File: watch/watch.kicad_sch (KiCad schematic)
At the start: 1 part, among them U1 nRF52840

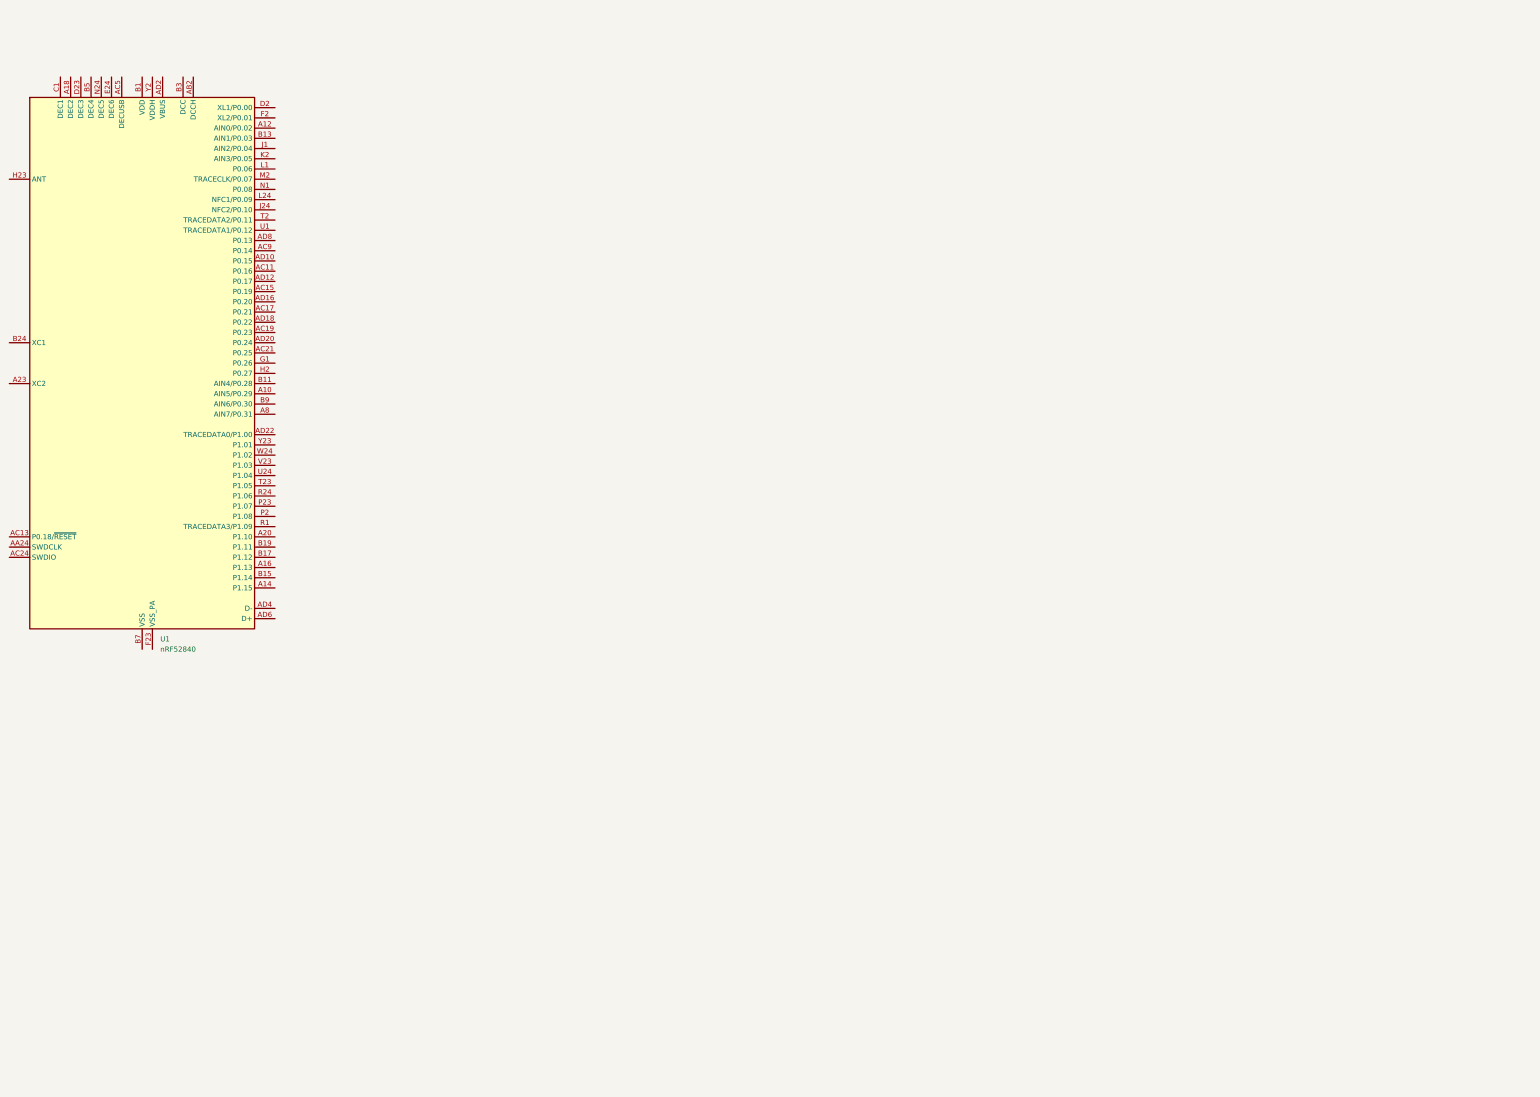
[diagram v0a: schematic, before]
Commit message: lots of stuff: power management, uC power, USB
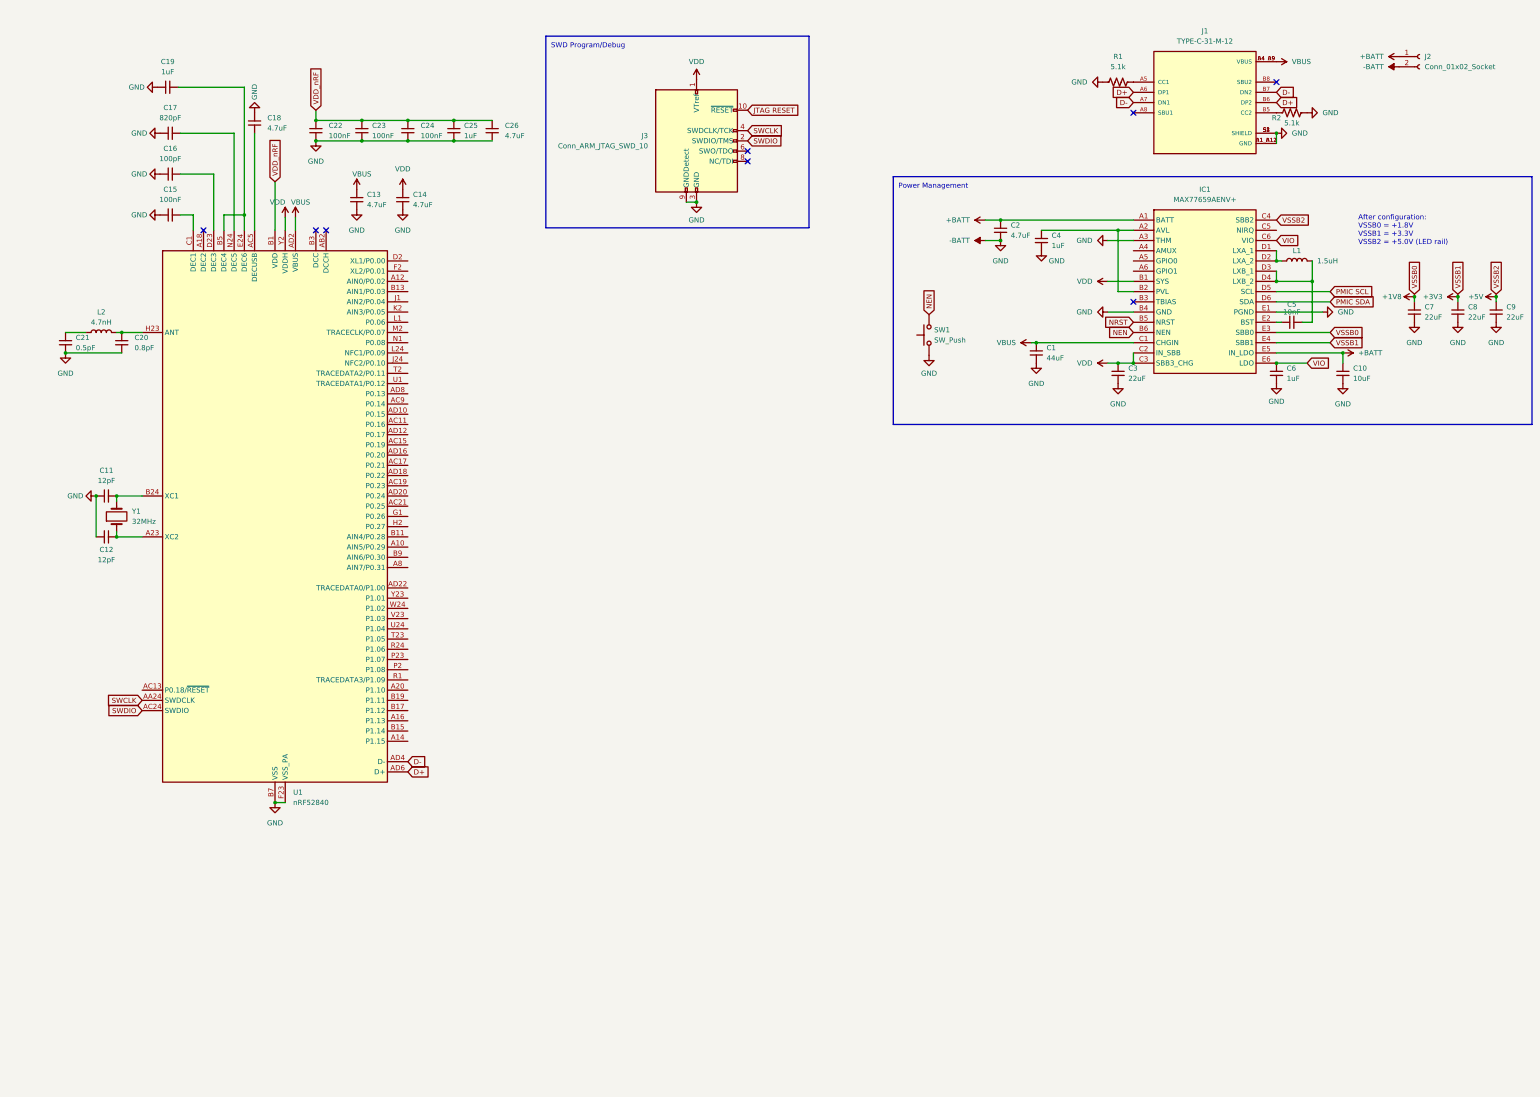
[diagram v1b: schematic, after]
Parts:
- added C1: 44uF, symbol Device:C_Small
- added C10: 10uF, symbol Device:C_Small
- added C11, C12: 12pF, symbol Device:C_Small
- added C13, C14, C18, C2, C26: 4.7uF, symbol Device:C_Small
- added C15, C22, C23, C24: 100nF, symbol Device:C_Small
- added C16: 100pF, symbol Device:C_Small
- added C17: 820pF, symbol Device:C_Small
- added C19, C25, C4, C6: 1uF, symbol Device:C_Small
- added C20: 0.8pF, symbol Device:C_Small
- added C21: 0.5pF, symbol Device:C_Small
- added C3, C7, C8, C9: 22uF, symbol Device:C_Small
- added C5: 10nF, symbol Device:C_Small
- added IC1: MAX77659AENV+, BGA30C40P6X5_255X237X50, symbol MAX77659AENV+:MAX77659AENV+
- added J1: TYPE-C-31-M-12, HRO_TYPE-C-31-M-12, symbol TYPE-C-31-M-12:TYPE-C-31-M-12
- added J2: Conn_01x02_Socket, symbol Connector:Conn_01x02_Socket
- added J3: Conn_ARM_JTAG_SWD_10, symbol Connector:Conn_ARM_JTAG_SWD_10
- added L1: 1.5uH, symbol Device:L
- added L2: 4.7nH, symbol Device:L
- added R1, R2: 5.1k, symbol Device:R_US
- added SW1: SW_Push, symbol Switch:SW_Push
- added Y1: 32MHz, symbol Device:Crystal
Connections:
- net VDD_nRF: now reaches U1.A22 (VDD), U1.AD14 (VDD), U1.AD23 (VDD), U1.B1 (VDD), U1.W1 (VDD)
- net VDD_nRF: now also C22.1, C23.1, C24.1, C25.1, C26.1
- net at U1.A23 (XC2): now also C12.1, Y1.1
- net SWCLK: now reaches U1.AA24 (SWDCLK)
- net SWCLK: now also J3.4 (SWDCLK/TCK)
- net SWDIO: now reaches U1.AC24 (SWDIO)
- net SWDIO: now also J3.2 (SWDIO/TMS)
- net at U1.AC5 (DECUSB): now also C18.2
- net VBUS: now reaches U1.AD2 (VBUS)
- net VBUS: now also C1.1, C13.1, IC1.C1 (CHGIN), J1.A4_B9 (VBUS), J1.B4_A9 (VBUS)
- net D-: now reaches U1.AD4 (D-)
- net D-: now also J1.A7 (DN1), J1.B7 (DN2)
- net D+: now reaches U1.AD6 (D+)
- net D+: now also J1.A6 (DP1), J1.B6 (DP2)
- net at U1.B24 (XC1): now also C11.2, Y1.2
- net at U1.B5 (DEC4): now also U1.E24 (DEC6), C19.2
- net -BATT: now reaches U1.B7 (VSS), U1.EP (VSS)
- net -BATT: now also U1.F23 (VSS_PA), C1.2, C10.2, C11.1, C12.2, C13.2, C14.2, C15.1, C16.1, C17.1, C18.1, C19.1, C2.2, C20.2, C21.2, C22.2, C23.2, C24.2, C25.2, C26.2, C3.2, C4.2, C6.2, C7.2, C8.2, C9.2, IC1.A3 (THM), IC1.B4 (GND), IC1.E1 (PGND), J1.A1_B12 (GND), J1.B1_A12 (GND), J1.S1 (SHIELD), J1.S2 (SHIELD), J1.S3 (SHIELD), J1.S4 (SHIELD), J2.2 (Pin_2), J3.3 (GND), J3.5 (GND), J3.9 (GNDDetect), R1.1, R2.1, SW1.1
- net at U1.C1 (DEC1): now also C15.2
- net at U1.D23 (DEC3): now also C16.2
- net at U1.H23 (ANT): now also C20.1, L2.2
- net at U1.N24 (DEC5): now also C17.2
- net VDD: now reaches U1.Y2 (VDDH)
- net VDD: now also C14.1, C3.1, IC1.B1 (SYS), IC1.C2 (IN_SBB), IC1.C3 (SBB3_CHG), J3.1 (VTref)
- new net: C21.1, L2.1
- new net: J1.B5 (CC2), R2.2
- new net: J1.A5 (CC1), R1.2
- new net: C4.1, IC1.A2 (AVL), IC1.B2 (PVL)
- new net: IC1.D1 (LXA_1), IC1.D2 (LXA_2), L1.1
- new net: C5.2, IC1.D3 (LXB_1), IC1.D4 (LXB_2), L1.2
- new net: C5.1, IC1.E2 (BST)
- new net +1V8: C7.1, IC1.E3 (SBB0)
- new net +3V3: C8.1, IC1.E4 (SBB1)
- new net +5V: C9.1, IC1.C4 (SBB2)
- new net +BATT: C10.1, C2.1, IC1.A1 (BATT), IC1.E5 (IN_LDO), J2.1 (Pin_1)
- new net JTAG RESET: J3.10 (~{RESET})
- new net NEN: IC1.B6 (NEN), SW1.2
- new net NRST: IC1.B5 (NRST)
- new net PMIC SCL: IC1.D5 (SCL)
- new net PMIC SDA: IC1.D6 (SDA)
- new net VIO: C6.1, IC1.C6 (VIO), IC1.E6 (LDO)
- no-connect marks 0 -> 8
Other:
- note added: "After configuration: VSSB0 = +1.8V VSSB1 = +3.3V VSSB2 = +5.0V (LED rail)"
- note added: "Power Management"
- note added: "SWD Program/Debug"
- moved on the sheet: U1

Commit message: organize and add display block, going to the gym
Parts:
- added C27, C29: 1uF, symbol Device:C_Small
- added C28: 100nF, symbol Device:C_Small
- added C30, C32: 10uF, symbol Device:C_Small
- added C31: 0.1uF, symbol Device:C_Small
- added D1, D2: VEMD5080X01, VEMD5080X01, symbol VEMD5080X01:VEMD5080X01
- added D3: CTDBLP31.12-6C5D-56-J6U6-20-R18, LED_CTDBLP31.12-6C5D-56-J6U6-20-R18, symbol CTDBLP31.12-6C5D-56-J6U6-20-R18:CTDBLP31.12-6C5D-56-J6U6-20-R18
- added IC2: MAX86141ENP+T, BGA20C40P5X4_205X185X50, symbol MAX86141ENP+T:MAX86141ENP+T
- added IC3: MAX32664GTGC+T, MAX32664GTGC, symbol MAX32664GTGC+T:MAX32664GTGC+T
- added J4: 505110-2291, 5051102291, symbol 505110-2291:505110-2291
- added Q1: BSS138, Package_TO_SOT_SMD:SOT-23, symbol Transistor_FET:BSS138
- added R3, R4, R5: 4.7k, symbol Device:R_US
- added R6, R7: 10, symbol Device:R_US
- added R8: R_US, symbol Device:R_US
- added Y2: 32.768kHz, symbol Device:Crystal
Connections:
- net +1V8: now also C30.2, C31.2, IC2.C2 (VDD_DIG), IC2.D2 (VDD_ANA), IC3.11 (VDD_1), IC3.22 (VDD_2), R3.1, R4.1, R5.1, R8.1
- net +5V: now also C32.2, D3.A, IC2.A1 (VLED)
- net -BATT: now also C27.1, C29.1, C30.1, C31.1, C32.1, D1.4 (A), D2.4 (A), IC2.C3 (GND_DIG), IC2.C4 (GND_ANA), IC2.C5 (PD_GND), IC2.D3 (PGND), IC3.10 (VSS_2), IC3.25 (EP), IC3.7 (VSS_1), J4.10 (DB4), J4.11 (DB3), J4.12 (DB2), J4.13 (DB1), J4.14 (DB0), J4.22 (GND), J4.23 (SUPP1), J4.24 (SUPP2), J4.5 (IM0), J4.7 (DB7), J4.8 (DB6), J4.9 (DB5), Q1.2 (S), R6.1; no longer C11.1, C12.2
- net JTAG RESET: now also U1.AC13 (P0.18/~{RESET})
- new net: Q1.3 (D), R7.2
- new net: C28.2, R6.2
- new net: IC3.8 (32KOUT), Y2.1
- new net: IC3.9 (32KIN), Y2.2
- new net: C27.2, IC3.12 (VCORE)
- new net: IC2.B2 (~{INT}), IC3.14 (PPG_INT), R3.2
- new net: IC2.A5 (CSB), IC3.18 (PPG_CS)
- new net: IC2.A2 (SCLK), IC3.19 (SENSOR_SCK)
- new net: IC2.A4 (SDI), IC3.20 (SENSOR_MOSI)
- new net: IC2.A3 (SDO), IC3.21 (SENSOR_MISO)
- new net: C29.2, IC2.B5 (VREF)
- new net +3.3V: J4.1 (LEDA), J4.3 (IM2), J4.4 (IM1), J4.6 (VCI)
- new net BIO MFIO: IC3.1 (MFIO)
- new net BIO RST: C28.1, IC3.6 (RSTN)
- new net BIO SCL: IC3.24 (SLAVE_SCL), R4.2
- new net BIO SDA: IC3.23 (SLAVE_SDA), R5.2
- new net BL ENABLE: Q1.1 (G), R8.2
- new net LED1_DRV: D3.C1, D3.C2, IC2.D1 (LED1_DRV)
- new net LEDK: J4.2 (LEDK), R7.1
- new net PD1: D1.1 (K_1), D1.2 (K_2), IC2.D5 (PD1_IN)
- new net PD2: D2.1 (K_1), D2.2 (K_2), IC2.D4 (PD2_IN)
- no-connect marks 8 -> 14
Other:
- note added: "Biometric sensors"
- note added: "TFT LCD"
- note added: "USB Type-C"
- note added: "nRF52840"
- moved on the sheet: C1, C10, C11, C12, C13, C14, C15, C16, C17, C18, C19, C2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

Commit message: first rev done
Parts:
- added C33: 100nF, symbol Device:C_Small
- added C34: 10nF, symbol Device:C_Small
- added C35: 2.2uF, symbol Device:C_Small
- added C36: 0.1uF, symbol Device:C_Small
- added IC4: TXS0108ERGYR, SN74LVC541ARGYR, symbol TXS0108ERGYR:TXS0108ERGYR
- added IC5: ~, symbol APX803:APX803
- added R10, R9: 10k, symbol Device:R_US
- added R11, R12: 4.7k, symbol Device:R_US
- added SW2, SW3, SW4, SW5: SW_Push, symbol Switch:SW_Push
- added U2: ICM-20602, Package_LGA:LGA-16_3x3mm_P0.5mm_LayoutBorder3x5y, symbol Sensor_Motion:ICM-20602
- R8: value R_US -> 10k
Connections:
- net BIO RST is gone; now on net ~{BIO RST}: C28.1, IC3.6 (RSTN)
- net BL ENABLE is gone; now on net ~{BL ENABLE}: Q1.1 (G), R8.2
- net NRST is gone; now on net ~{PMIC RST}: IC1.B5 (NRST)
- net PMIC SCL is gone; now on net AX SCL: IC1.D5 (SCL)
- net PMIC SDA is gone; now on net AX SDA: IC1.D6 (SDA)
- net +1V8: now also C33.1, C34.1, C35.1, IC4.19 (VCCB), IC5.3 (VCC), R10.1, R11.1, R12.1, R9.1, U2.1 (VDDIO), U2.16 (VDD), U2.5 (~{CS})
- net +3V3: now also IC4.10 (OE), IC4.2 (VCCA)
- net -BATT: now also C11.1, C12.2, J4.15 (RD), C33.2, C34.2, C35.2, C36.2, IC4.11 (GND), IC4.21 (EP), IC5.1 (GND), SW2.1, SW3.1, SW4.1, SW5.1, U2.10 (GND), U2.11 (GND), U2.12 (GND), U2.13 (GND), U2.15 (GND), U2.4 (SAO/SD0), U2.8 (FSYNC), U2.9 (GND)
- net BIO MFIO: now also U1.AD16 (P0.20)
- net DC 3V: now reaches J4.16 (WR)
- net DC 3V: now also IC4.3 (A2)
- net SCK 3V: now reaches J4.17 (RS)
- net SCK 3V: now also IC4.4 (A3)
- net CS 3V: now reaches J4.18 (CS)
- net CS 3V: now also IC4.6 (A5)
- net TE 3V: now reaches J4.19 (TE)
- net TE 3V: now also IC4.7 (A6)
- net ~{TFTRST}: now reaches J4.20 (RESET)
- net ~{TFTRST}: now also IC4.8 (A7)
- net SDA 3V: now reaches J4.21 (SDA)
- net SDA 3V: now also IC4.5 (A4)
- net PMIC GPIO2: now reaches U1.A10 (AIN5/P0.29)
- net PMIC GPIO2: now also IC1.A5 (GPIO0)
- net PMIC AMUX: now reaches U1.A12 (AIN0/P0.02)
- net PMIC AMUX: now also IC1.A4 (AMUX)
- net TFTCS: now reaches U1.AC11 (P0.16)
- net TFTCS: now also IC4.15 (B5), R10.2
- net ~{BL ENABLE}: now reaches U1.AC15 (P0.19)
- net ~{BIO RST}: now reaches U1.AC17 (P0.21)
- net ~{TFTRST} 1V8: now reaches U1.AC19 (P0.23)
- net ~{TFTRST} 1V8: now also IC4.13 (B7), IC5.2 (~{RESET}), R9.2
- net ~{PMIC IRQ}: now reaches U1.AC21 (P0.25)
- net ~{PMIC IRQ}: now also IC1.C5 (NIRQ), R12.2
- net TFTSCK: now reaches U1.AC9 (P0.14)
- net TFTSCK: now also IC4.17 (B3)
- net TFTDC: now reaches U1.AD10 (P0.15)
- net TFTDC: now also IC4.18 (B2)
- net TFTTE: now reaches U1.AD12 (P0.17)
- net TFTTE: now also IC4.14 (B6)
- net AX IRQ: now reaches U1.AD18 (P0.22)
- net AX IRQ: now also U2.6 (INT)
- net ~{PMIC RST}: now reaches U1.AD20 (P0.24)
- net ~{PMIC RST}: now also R4.2
- net TFTMOSI: now reaches U1.AD8 (P0.13)
- net TFTMOSI: now also IC4.16 (B4)
- net PMIC GPIO1: now reaches U1.B11 (AIN4/P0.28)
- net PMIC GPIO1: now also IC1.A6 (GPIO1)
- net AX SCL: now reaches U1.T2 (TRACEDATA2/P0.11)
- net AX SCL: now also IC3.24 (SLAVE_SCL), R5.2, U2.2 (SCL/SPC)
- net AX SDA: now reaches U1.U1 (TRACEDATA1/P0.12)
- net AX SDA: now also IC3.23 (SLAVE_SDA), R11.2, U2.3 (SDA/SDI)
- net S4: now reaches U1.U24 (P1.04)
- net S4: now also SW5.2
- net S3: now reaches U1.V23 (P1.03)
- net S3: now also SW4.2
- net S2: now reaches U1.W24 (P1.02)
- net S2: now also SW3.2
- net S1: now reaches U1.Y23 (P1.01)
- net S1: now also SW2.2
- removed net BIO SCL: IC3.24 (SLAVE_SCL), R4.2
- removed net BIO SDA: IC3.23 (SLAVE_SDA), R5.2
- net NEN renamed ~{PMIC EN}
- new net: C36.1, U2.14 (REGOUT)
- no-connect marks 14 -> 18
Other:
- note added: "HID"
- moved on the sheet: C1, C10, C2, C27, C28, C29, C3, C30, C31, C32, C4, C5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

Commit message: parts finalized, started routing
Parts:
- removed SW1, SW2, SW3, SW4, SW5: SW_Push, symbol Switch:SW_Push
- removed Y1: 32MHz, symbol Device:Crystal
- removed Y2: 32.768kHz, symbol Device:Crystal
- added LED1, LED2, LED3, LED4, LED5: VLMO20J2M1-GS08, VLMO20J2M1-GS08:LEDM2214X140N, symbol VLMO20J2M1-GS08:VLMO20J2M1-GS08
- added R13: 100, Resistor_SMD:R_0805_2012Metric_Pad1.20x1.40mm_HandSolder, symbol Device:R_US
- added R14: 200, Resistor_SMD:R_0805_2012Metric_Pad1.20x1.40mm_HandSolder, symbol Device:R_US
- added S1, S2, S3, S4, S5: EVP-ATAL1B000, EVP-ATAL1B000:EVPATAL1B000, symbol EVP-ATAL1B000:EVP-ATAL1B000
- added TP1, TP10, TP11, TP12, TP13, TP14, TP15, TP16, TP17, TP18, TP19, TP2, TP20, TP21, TP22, TP23, TP24, TP25, TP26, TP27, TP28, TP29, TP3, TP30, TP31, TP32, TP33, TP34, TP35, TP36, TP37, TP38, TP39, TP4, TP5, TP6, TP7, TP8, TP9: TestPoint, TestPoint:TestPoint_Pad_D2.0mm, symbol Connector:TestPoint
- added Y1: FA-128_32.0000MF10Z-AJ5, FA-128_32.0000MF10Z-AJ5:FA128320000MF10ZAJ5, symbol FA-128_32_0000MF10Z-AJ5:FA-128_32.0000MF10Z-AJ5
- added Y2: CM7V-T1A-32.768kHz-6pF-20PPM-TA-QC, CM7V-T1A-32.768kHz-6pF-20PPM-TA-QC:CM7V32768TBQA020, symbol CM7V-T1A-32_768kHz-6pF-20PPM-T:CM7V-T1A-32.768kHz-6pF-20PPM-TA-QC
- C1, C10, C13, C14, C18, C19, C2, C25, C26, C27, C29, C3, C30, C32, C35, C7, C8, C9: footprint (none) -> Capacitor_SMD:C_0603_1608Metric_Pad1.08x0.95mm_HandSolder
- C11, C12, C15, C16, C17, C20, C21, C22, C23, C24, C28, C31, C33, C34, C36, C4, C6: footprint (none) -> Capacitor_SMD:C_0402_1005Metric_Pad0.74x0.62mm_HandSolder
- C5: footprint (none) -> Capacitor_SMD:C_0201_0603Metric_Pad0.64x0.40mm_HandSolder
- D1, D2: footprint VEMD5080X01 -> VEMD5080X01:VEMD5080X01
- D3: footprint LED_CTDBLP31.12-6C5D-56-J6U6-20-R18 -> ctdblp31.12:LED_CTDBLP31.12-6C5D-56-J6U6-20-R18
- IC1: footprint BGA30C40P6X5_255X237X50 -> MAX77659:BGA30C40P6X5_255X237X50
- IC2: footprint BGA20C40P5X4_205X185X50 -> MAX86141:BGA20C40P5X4_205X185X50
- IC3: footprint MAX32664GTGC -> MAX32664:MAX32664GTGC
- IC4: footprint SN74LVC541ARGYR -> TXS0108ERGYR:SN74LVC541ARGYR
- IC5: footprint (none) -> Package_TO_SOT_SMD:SOT-23-3
- J1: footprint HRO_TYPE-C-31-M-12 -> type-c-31-m-12:HRO_TYPE-C-31-M-12
- J2: footprint (none) -> Connector_PinHeader_2.54mm:PinHeader_1x02_P2.54mm_Vertical
- J3: footprint (none) -> Connector_PinHeader_2.54mm:PinHeader_2x05_P2.54mm_Vertical
- J4: footprint 5051102291 -> 505110-2291:5051102291
- L1: footprint (none) -> Inductor_SMD:L_0603_1608Metric_Pad1.05x0.95mm_HandSolder
- L2: footprint (none) -> Inductor_SMD:L_0402_1005Metric_Pad0.77x0.64mm_HandSolder
- R1, R10, R11, R12, R2, R3, R4, R5, R6, R8, R9: footprint (none) -> Resistor_SMD:R_0201_0603Metric_Pad0.64x0.40mm_HandSolder
- R7: footprint (none) -> Resistor_SMD:R_0805_2012Metric_Pad1.20x1.40mm_HandSolder
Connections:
- net +1V8: now also LED1.2 (A), TP5.1; no longer U2.5 (~{CS})
- net +3V3: now also LED2.2 (A), TP4.1
- net +5V: now also LED3.2 (A), TP3.1
- net +BATT: now also TP24.1
- net -BATT: now also C11.2, LED1.1 (K), LED4.1 (K), LED5.1 (K), R13.2, R14.2, S1.2 (COM), S1.MH1, S1.MH2, S1.MP1, S1.MP2, S1.MP3, S2.2 (COM), S2.MH1, S2.MH2, S2.MP1, S2.MP2, S2.MP3, S3.2 (COM), S3.MH1, S3.MH2, S3.MP1, S3.MP2, S3.MP3, S4.2 (COM), S4.MH1, S4.MH2, S4.MP1, S4.MP2, S4.MP3, S5.2 (COM), S5.MH1, S5.MH2, S5.MP1, S5.MP2, S5.MP3, TP25.1, Y1.2 (GROUND_1), Y1.4 (GROUND_2); no longer C11.1
- net AX SCL: now also TP2.1
- net AX SDA: now also TP1.1
- net CS 3V: now also TP9.1
- net D+: now also TP27.1
- net D-: now also TP26.1
- net DC 3V: now also TP6.1
- net LEDK: now also TP13.1
- net PD1: now also TP17.1
- net PD2: now also TP18.1
- net S1: now also S1.1 (NO)
- net S2: now also S3.1 (NO)
- net S3: now also S2.1 (NO)
- net S4: now also S4.1 (NO)
- net SCK 3V: now also TP7.1
- net SDA 3V: now also TP8.1
- net TE 3V: now also TP10.1
- net TFTCS: now also TP31.1
- net TFTDC: now also TP34.1
- net TFTMOSI: now also TP32.1
- net TFTSCK: now also TP33.1
- net TFTTE: now also TP30.1
- net VDD: now also TP28.1; no longer J3.1 (VTref)
- net VDD_nRF: now also J3.1 (VTref)
- net VIO: now also TP14.1
- net ~{BIO RST}: now also TP39.1
- net ~{BL ENABLE}: now also TP12.1
- net ~{PMIC EN}: now also S5.1 (NO), TP16.1
- net ~{PMIC IRQ}: now also TP38.1
- net ~{PMIC RST}: now also TP15.1, TP37.1
- net ~{TFTRST}: now also TP11.1
- net ~{TFTRST} 1V8: now also U1.G1 (P0.26), TP29.1; no longer U1.AC19 (P0.23)
- net at IC3.8 (32KOUT): now also Y2.2
- net at IC3.9 (32KIN): now also Y2.1
- net LED1: now reaches U1.A16 (P1.13)
- net LED1: now also LED4.2 (A)
- net at C12.1, U1.A23 (XC2): now also Y1.3 (CRYSTAL_2)
- net LED2: now reaches U1.B15 (P1.14)
- net LED2: now also LED5.2 (A)
- net at U1.B24 (XC1): now also C11.1, Y1.1 (CRYSTAL_1); no longer C11.2
- net at IC2.B2 (~{INT}), IC3.14 (PPG_INT), R3.2: now also TP19.1
- net at IC2.A5 (CSB), IC3.18 (PPG_CS): now also TP21.1
- net at IC2.A2 (SCLK), IC3.19 (SENSOR_SCK): now also TP20.1
- net at IC2.A4 (SDI), IC3.20 (SENSOR_MOSI): now also TP23.1
- net at IC2.A3 (SDO), IC3.21 (SENSOR_MISO): now also TP22.1
- net at C5.2, IC1.D3 (LXB_1), IC1.D4 (LXB_2)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: now also TP36.1
- new net: LED3.1 (K), R14.1
- new net: LED2.1 (K), R13.1
- new net AX AD0: TP35.1, U1.AC19 (P0.23), U2.5 (~{CS})
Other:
- note added: "Indicators"
- moved on the sheet: C11, C12
